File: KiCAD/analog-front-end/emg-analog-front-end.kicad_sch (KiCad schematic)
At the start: 42 parts, among them J1 Conn_01x03, J2 Conn_01x03, J4 Conn_01x03_Female, J5 Conn_01x03_Female, J6 Conn_01x03_Female, J7 Conn_01x03_Female, U1 AD620, U2 LMC6482, U3 LMC6482, U4 LMC6482

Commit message: more progress on layout
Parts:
- added J3: Conn_01x03, Connector_PinHeader_1.27mm:PinHeader_1x03_P1.27mm_Vertical, symbol Connector_Generic:Conn_01x03
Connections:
- net AOUT_CH0: now also J3.2 (Pin_2)
- net GND: now also J3.1 (Pin_1)
- net VDD: now also J3.3 (Pin_3)
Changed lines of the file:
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@@
   (junction (at 259.4864 64.7192) (diameter 0) (color 0 0 0 0)
   )
+  (junction (at 228.6 132.5372) (diameter 0) (color 0 0 0 0)
+  )
   (junction (at 423.8752 105.4608) (diameter 0) (color 0 0 0 0)
   )
@@
   )
   (junction (at 142.6464 73.2282) (diameter 0) (color 0 0 0 0)
+  )
+  (junction (at 228.6 132.5118) (diameter 0) (color 0 0 0 0)
   )
   (junction (at 35.3314 80.2132) (diameter 0) (color 0 0 0 0)
@@
     (stroke (width 0) (type default) (color 0 0 0 0))
   )
+  (wire (pts (xy 228.6 132.5118) (xy 228.6 132.5372))
+    (stroke (width 0) (type default) (color 0 0 0 0))
+  )
   (wire (pts (xy 86.2076 121.7422) (xy 86.2076 122.8852))
     (stroke (width 0) (type default) (color 0 0 0 0))
@@
     (stroke (width 0) (type default) (color 0 0 0 0))
   )
+  (wire (pts (xy 260.9088 134.9756) (xy 262.8392 134.9756))
+    (stroke (width 0) (type default) (color 0 0 0 0))
+  )
   (wire (pts (xy 71.5264 67.0052) (xy 71.5264 72.0852))
     (stroke (width 0) (type default) (color 0 0 0 0))
@@
     (stroke (width 0) (type default) (color 0 0 0 0))
   )
+  (wire (pts (xy 260.2738 132.4356) (xy 262.8392 132.4356))
+    (stroke (width 0) (type default) (color 0 0 0 0))
+  )
   (wire (pts (xy 204.8764 74.2442) (xy 200.4314 74.2442))
     (stroke (width 0) (type default) (color 0 0 0 0))
@@
     (stroke (width 0) (type default) (color 0 0 0 0))
   )
+  (wire (pts (xy 261.112 129.8956) (xy 262.8392 129.8956))
+    (stroke (width 0) (type default) (color 0 0 0 0))
+  )
   (wire (pts (xy 77.7494 122.8852) (xy 81.1276 122.8852))
     (stroke (width 0) (type default) (color 0 0 0 0))
@@
     (stroke (width 0) (type default) (color 0 0 0 0))
   )
+  (wire (pts (xy 227.1014 132.5118) (xy 228.6 132.5118))
+    (stroke (width 0) (type default) (color 0 0 0 0))
+  )
   (wire (pts (xy 81.1276 121.7422) (xy 81.1276 122.8852))
     (stroke (width 0) (type default) (color 0 0 0 0))
@@
   )
   (wire (pts (xy 108.4834 56.2102) (xy 111.0234 56.2102))
+    (stroke (width 0) (type default) (color 0 0 0 0))
+  )
+  (wire (pts (xy 261.112 128.1938) (xy 261.112 129.8956))
     (stroke (width 0) (type default) (color 0 0 0 0))
   )
@@
     )
   )
+  (global_label "AOUT_CH0" (shape input) (at 260.2738 132.4356 180) (fields_autoplaced)
+    (effects (font (size 1.27 1.27)) (justify right))
+    (property "Intersheet References" "${INTERSHEET_REFS}" (id 0) (at 248.3659 132.3562 0)
+      (effects (font (size 1.27 1.27)) (justify right) hide)
+    )
+  )
+  (global_label "AOUT_CH0" (shape input) (at 227.1014 132.5118 180) (fields_autoplaced)
+    (effects (font (size 1.27 1.27)) (justify right))
+    (property "Intersheet References" "${INTERSHEET_REFS}" (id 0) (at 215.1935 132.4324 0)
+      (effects (font (size 1.27 1.27)) (justify right) hide)
+    )
+  )
+  (symbol (lib_id "power:VDD") (at 260.9088 134.9756 90) (unit 1)
+    (in_bom yes) (on_board yes) (fields_autoplaced)
+    (property "Reference" "#PWR03" (id 0) (at 264.7188 134.9756 0)
+      (effects (font (size 1.27 1.27)) hide)
+    )
+    (property "Value" "VDD" (id 1) (at 257.683 134.9755 90)
+      (effects (font (size 1.27 1.27)) (justify left))
+    )
+    (property "Footprint" "" (id 2) (at 260.9088 134.9756 0)
+      (effects (font (size 1.27 1.27)) hide)
+    )
+    (property "Datasheet" "" (id 3) (at 260.9088 134.9756 0)
+      (effects (font (size 1.27 1.27)) hide)
+    )
+    (pin "1")
+  )
   (symbol (lib_id "pspice:C") (at 102.1334 56.2102 270) (unit 1)
     (in_bom yes) (on_board yes)
@@
     (pin "2")
     (pin "3")
+  )
+  (symbol (lib_id "power:GND") (at 261.112 128.1938 180) (unit 1)
+    (in_bom yes) (on_board yes) (fields_autoplaced)
+    (property "Reference" "#PWR019" (id 0) (at 261.112 121.8438 0)
+      (effects (font (size 1.27 1.27)) hide)
+    )
+    (property "Value" "GND" (id 1) (at 261.112 122.682 0))
+    (property "Footprint" "" (id 2) (at 261.112 128.1938 0)
+      (effects (font (size 1.27 1.27)) hide)
+    )
+    (property "Datasheet" "" (id 3) (at 261.112 128.1938 0)
+      (effects (font (size 1.27 1.27)) hide)
+    )
+    (pin "1")
   )
   (symbol (lib_id "Amplifier_Operational:LMC6482") (at 53.4162 122.8852 0) (unit 1)
@@
     (pin "2")
   )
+  (symbol (lib_id "Connector_Generic:Conn_01x03") (at 267.9192 132.4356 0) (unit 1)
+    (in_bom yes) (on_board yes)
+    (property "Reference" "J3" (id 0) (at 267.7922 127.127 0))
+    (property "Value" "Conn_01x03" (id 1) (at 263.8552 138.7856 0)
+      (effects (font (size 1.27 1.27)) hide)
+    )
+    (property "Footprint" "Connector_PinHeader_1.27mm:PinHeader_1x03_P1.27mm_Vertical" (id 2) (at 267.9192 132.4356 0)
+      (effects (font (size 1.27 1.27)) hide)
+    )
+    (property "Datasheet" "~" (id 3) (at 267.9192 132.4356 0)
+      (effects (font (size 1.27 1.27)) hide)
+    )
+    (pin "1")
+    (pin "2")
+    (pin "3")
+  )
   (symbol (lib_id "Amplifier_Operational:LMC6482") (at 41.6814 164.4396 0) (unit 2)
     (in_bom yes) (on_board yes) (fields_autoplaced)
@@
       (reference "#PWR02") (unit 1) (value "GND") (footprint "")
     )
+    (path "/01222a78-3c9b-4f9a-8485-95c2b5f1ec36"
+      (reference "#PWR03") (unit 1) (value "VDD") (footprint "")
+    )
     (path "/296a6d8c-2096-47b5-aaa1-f04a44b3ff87"
       (reference "#PWR04") (unit 1) (value "VDD") (footprint "")
@@
       (reference "#PWR018") (unit 1) (value "GND") (footprint "")
     )
+    (path "/8abb0df5-5035-45cd-87c6-8da2c46cb897"
+      (reference "#PWR019") (unit 1) (value "GND") (footprint "")
+    )
     (path "/3e432ac1-b0f6-4fa6-a99e-a993b71b6831"
       (reference "#PWR020") (unit 1) (value "GND") (footprint "")
@@
       (reference "J2") (unit 1) (value "Conn_01x03") (footprint "Connector_PinHeader_1.27mm:PinHeader_1x03_P1.27mm_Vertical")
     )
+    (path "/c23949b2-419b-4b01-9aa6-519bd8127198"
+      (reference "J3") (unit 1) (value "Conn_01x03") (footprint "Connector_PinHeader_1.27mm:PinHeader_1x03_P1.27mm_Vertical")
+    )
     (path "/153c98c9-b424-44a6-9b60-24a3ab4bb483"

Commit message: AFE sub-circuit layout done
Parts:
- J4, J5, J6, J7: footprint Connector_PinHeader_1.27mm:PinHeader_1x03_P1.27mm_Vertical -> Connector_PinHeader_2.54mm:PinHeader_1x03_P2.54mm_Vertical
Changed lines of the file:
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@@
       (effects (font (size 1.27 1.27)) (justify left) hide)
     )
-    (property "Footprint" "Connector_PinHeader_1.27mm:PinHeader_1x03_P1.27mm_Vertical" (id 2) (at 70.8914 130.0226 0)
+    (property "Footprint" "Connector_PinHeader_2.54mm:PinHeader_1x03_P2.54mm_Vertical" (id 2) (at 70.8914 130.0226 0)
       (effects (font (size 1.27 1.27)) hide)
     )
@@
       (effects (font (size 1.27 1.27)) (justify left) hide)
     )
-    (property "Footprint" "Connector_PinHeader_1.27mm:PinHeader_1x03_P1.27mm_Vertical" (id 2) (at 83.6676 130.2766 0)
+    (property "Footprint" "Connector_PinHeader_2.54mm:PinHeader_1x03_P2.54mm_Vertical" (id 2) (at 83.6676 130.2766 0)
       (effects (font (size 1.27 1.27)) hide)
     )
@@
       (effects (font (size 1.27 1.27)) (justify left) hide)
     )
-    (property "Footprint" "Connector_PinHeader_1.27mm:PinHeader_1x03_P1.27mm_Vertical" (id 2) (at 186.7154 141.2494 0)
+    (property "Footprint" "Connector_PinHeader_2.54mm:PinHeader_1x03_P2.54mm_Vertical" (id 2) (at 186.7154 141.2494 0)
       (effects (font (size 1.27 1.27)) hide)
     )
@@
       (effects (font (size 1.27 1.27)) (justify left) hide)
     )
-    (property "Footprint" "Connector_PinHeader_1.27mm:PinHeader_1x03_P1.27mm_Vertical" (id 2) (at 154.5844 78.3844 0)
+    (property "Footprint" "Connector_PinHeader_2.54mm:PinHeader_1x03_P2.54mm_Vertical" (id 2) (at 154.5844 78.3844 0)
       (effects (font (size 1.27 1.27)) hide)
     )
@@
     )
     (path "/153c98c9-b424-44a6-9b60-24a3ab4bb483"
-      (reference "J4") (unit 1) (value "Conn_01x03_Female") (footprint "Connector_PinHeader_1.27mm:PinHeader_1x03_P1.27mm_Vertical")
+      (reference "J4") (unit 1) (value "Conn_01x03_Female") (footprint "Connector_PinHeader_2.54mm:PinHeader_1x03_P2.54mm_Vertical")
     )
     (path "/3a2fee8a-0cad-4896-9f41-da70be9ba6f1"
-      (reference "J5") (unit 1) (value "Conn_01x03_Female") (footprint "Connector_PinHeader_1.27mm:PinHeader_1x03_P1.27mm_Vertical")
+      (reference "J5") (unit 1) (value "Conn_01x03_Female") (footprint "Connector_PinHeader_2.54mm:PinHeader_1x03_P2.54mm_Vertical")
     )
     (path "/b7ea6100-ff11-4609-86f6-89b95a0d171e"
-      (reference "J6") (unit 1) (value "Conn_01x03_Female") (footprint "Connector_PinHeader_1.27mm:PinHeader_1x03_P1.27mm_Vertical")
+      (reference "J6") (unit 1) (value "Conn_01x03_Female") (footprint "Connector_PinHeader_2.54mm:PinHeader_1x03_P2.54mm_Vertical")
     )
     (path "/575236b7-a07a-470e-adbc-ea724e1ab06d"
-      (reference "J7") (unit 1) (value "Conn_01x03_Female") (footprint "Connector_PinHeader_1.27mm:PinHeader_1x03_P1.27mm_Vertical")
+      (reference "J7") (unit 1) (value "Conn_01x03_Female") (footprint "Connector_PinHeader_2.54mm:PinHeader_1x03_P2.54mm_Vertical")
     )
     (path "/454ea407-2f72-4fa0-894f-85a6430a855f"

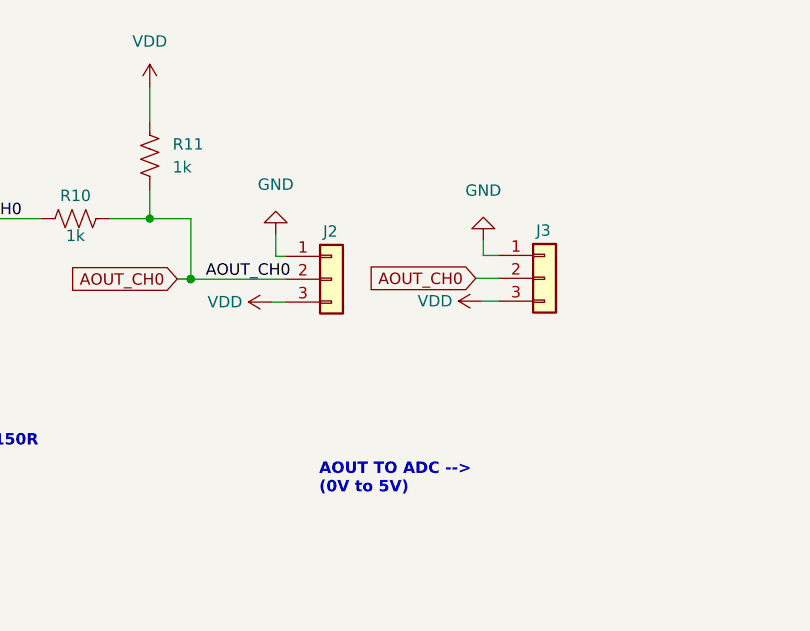
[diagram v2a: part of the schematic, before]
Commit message: added VSS input to the AFE board
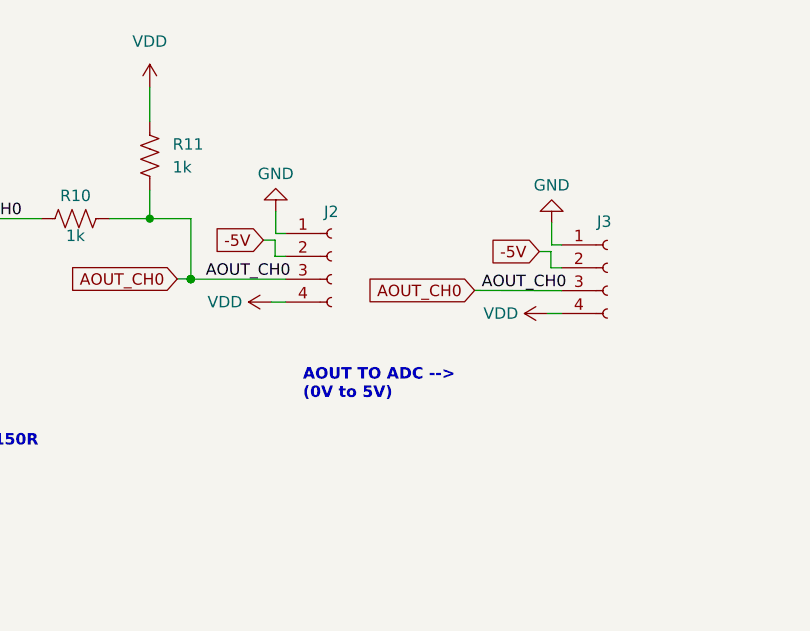
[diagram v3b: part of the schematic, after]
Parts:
- removed J2, J3: Conn_01x03, Connector_PinHeader_1.27mm:PinHeader_1x03_P1.27mm_Vertical, symbol Connector_Generic:Conn_01x03
- added J2, J3: Conn_01x04_Female, Connector_PinHeader_1.27mm:PinHeader_1x04_P1.27mm_Vertical, symbol Connector:Conn_01x04_Female
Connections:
- net -5V: now also J2.2 (Pin_2), J3.2 (Pin_2)
- net AOUT_CH0: now also J2.3 (Pin_3), J3.3 (Pin_3)
- net GND: now also J2.1 (Pin_1), J3.1 (Pin_1)
- net VDD: now also J2.4 (Pin_4), J3.4 (Pin_4)

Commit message: replaced temporary resistor holders and added voltage inverter IC
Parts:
- removed J4, J5, J6, J7: Conn_01x03_Female, Connector_PinHeader_2.54mm:PinHeader_1x03_P2.54mm_Vertical, symbol Connector:Conn_01x03_Female
- added C? (x2): 1uF, Capacitor_SMD:C_0402_1005Metric, symbol pspice:C
- added R3, R5: 75R, Resistor_SMD:R_0402_1005Metric, symbol Device:R_US
- added R6: 75k, Resistor_SMD:R_0402_1005Metric, symbol Device:R_US
- added R7: 510R, Resistor_SMD:R_0402_1005Metric, symbol Device:R_US
- added U?: MAX1697REUT+T, SOT95P280X145-6N, symbol MAX1697REUT_T:MAX1697REUT+T
- U2, U3, U4: value LMC6482 -> LMC6492
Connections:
- net AMP_IN-_CH0: now also R7.1
- net GND: now also C?.1, R6.2, R7.2, U?.4 (GND)
- net HPF_OUT_CH0: now also R6.1
- net SK00: now also R3.2
- net SK01: now also R3.1, R5.2
- net SK11: now also R5.1
- net VDD: now also J2.2 (Pin_2), J3.2 (Pin_2), U?.2 (IN), U?.5 (~{SHDN}); no longer J2.4 (Pin_4), J3.4 (Pin_4)
- net -5V renamed -VDD
- net -VDD: now also J2.4 (Pin_4), J3.4 (Pin_4), C?.2, U?.1 (OUT); no longer J2.2 (Pin_2), J3.2 (Pin_2)
- new net: C?.1, U?.3 (C1-)
- new net: C?.2, U?.6 (C1+)
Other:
- note added: "AOUT TO ADC --> (GND to VDD)"
- note added: "GAIN = 197 with R = 510R"
- note removed: "AOUT TO ADC --> (0V to 5V)"
- note removed: "GAIN = 668 with R = 150R"
